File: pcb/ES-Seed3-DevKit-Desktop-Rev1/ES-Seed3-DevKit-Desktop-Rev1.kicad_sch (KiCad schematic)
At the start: 0 parts

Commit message: schematic is like 85% done.. just needs audio circuits, and opamp choice(s).
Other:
- removed sheet Power
- sheet Daisy: file Seed3-DevKit-Eurorack_1.kicad_sch -> Seed3-DevKit-Desktop_1.kicad_sch
- sheet Peripherals: file Seed3-DevKit-Eurorack_2.kicad_sch -> Seed3-DevKit-Desktop_2.kicad_sch
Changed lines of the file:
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@@
 			)
 		)
-		(property "Sheetfile" "Seed3-DevKit-Eurorack_2.kicad_sch"
+		(property "Sheetfile" "Seed3-DevKit-Desktop_2.kicad_sch"
 			(at 76.2 29.7946 0)
 			(effects
@@
 		)
 		(instances
-			(project "Seed3-DevKit-Eurorack-Rev1"
+			(project "ES-Seed3-DevKit-Desktop-Rev1"
 				(path "/19edde5c-efb5-4a72-a9f3-fb5a3c99bba0"
 					(page "2")
-				)
-			)
-		)
-	)
-	(sheet
-		(at 177.8 25.4)
-		(size 12.7 3.81)
-		(exclude_from_sim no)
-		(in_bom yes)
-		(on_board yes)
-		(dnp no)
-		(fields_autoplaced yes)
-		(stroke
-			(width 0)
-			(type solid)
-		)
-		(fill
-			(color 0 0 0 0.0000)
-		)
-		(property "Sheetname" "Power"
-			(at 177.8 24.6884 0)
-			(effects
-				(font
-					(size 1.27 1.27)
-				)
-				(justify left bottom)
-			)
-		)
-		(property "Sheetfile" "Seed3-DevKit-Eurorack_4.kicad_sch"
-			(at 177.8 29.7946 0)
-			(effects
-				(font
-					(size 1.27 1.27)
-				)
-				(justify left top)
-			)
-		)
-		(instances
-			(project "Seed3-DevKit-Eurorack-Rev1"
-				(path "/19edde5c-efb5-4a72-a9f3-fb5a3c99bba0"
-					(page "4")
 				)
 			)
@@
 			)
 		)
-		(property "Sheetfile" "Seed3-DevKit-Eurorack_1.kicad_sch"
+		(property "Sheetfile" "Seed3-DevKit-Desktop_1.kicad_sch"
 			(at 25.4 29.7946 0)
 			(effects
@@
 		)
 		(instances
-			(project "Seed3-DevKit-Eurorack-Rev1"
+			(project "ES-Seed3-DevKit-Desktop-Rev1"
 				(path "/19edde5c-efb5-4a72-a9f3-fb5a3c99bba0"
 					(page "1")

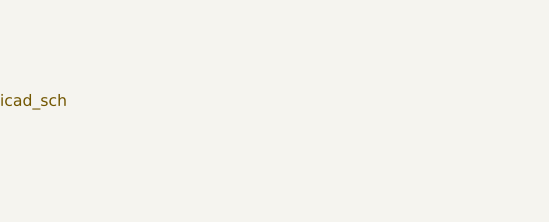
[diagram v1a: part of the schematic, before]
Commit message: sch complete (pending value changes to audio out circuit and ERC fixes), footprints set, ready for layout.
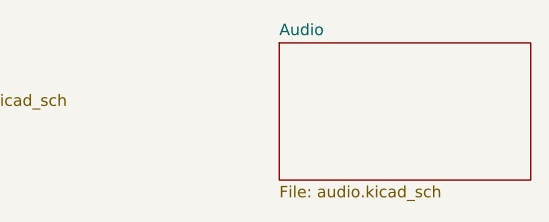
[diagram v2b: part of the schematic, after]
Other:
- added sheet Audio (audio.kicad_sch)
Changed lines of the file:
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@@
+		)
+	)
+	(sheet
+		(at 134.62 24.13)
+		(size 27.94 15.24)
+		(exclude_from_sim no)
+		(in_bom yes)
+		(on_board yes)
+		(dnp no)
+		(fields_autoplaced yes)
+		(stroke
+			(width 0.1524)
+			(type solid)
+		)
+		(fill
+			(color 0 0 0 0.0000)
+		)
+		(property "Sheetname" "Audio"
+			(at 134.62 23.4184 0)
+			(effects
+				(font
+					(size 1.27 1.27)
+				)
+				(justify left bottom)
+			)
+		)
+		(property "Sheetfile" "audio.kicad_sch"
+			(at 134.62 39.9546 0)
+			(effects
+				(font
+					(size 1.27 1.27)
+				)
+				(justify left top)
+			)
+		)
+		(instances
+			(project "ES-Seed3-DevKit-Desktop-Rev1"
+				(path "/19edde5c-efb5-4a72-a9f3-fb5a3c99bba0"
+					(page "4")
+				)
+			)
 		)
 	)

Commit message: pre-routing checkpoint.
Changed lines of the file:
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@@
 	)
 	(sheet
-		(at 134.62 24.13)
+		(at 147.32 48.26)
 		(size 27.94 15.24)
 		(exclude_from_sim no)
@@
 		)
 		(property "Sheetname" "Audio"
-			(at 134.62 23.4184 0)
+			(at 147.32 47.5484 0)
 			(effects
 				(font
@@
 		)
 		(property "Sheetfile" "audio.kicad_sch"
-			(at 134.62 39.9546 0)
+			(at 147.32 64.0846 0)
 			(effects
 				(font
